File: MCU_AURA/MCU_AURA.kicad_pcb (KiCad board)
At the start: 4 copper layers, 50 x 50 mm, 110 parts, among them IC1 PCA9685PW,118, IC2 W25Q128JVSIQ, J1 TF-CARD_H1.8, J100 USB_C_Receptacle_USB2.0_16P, J400 532617004, J401 532617004, J402 532617004, J403 532617012, J404 532617007, J405 532617007, J406 532617012, J407 532617007, J408 532617004, Q300 BSS138, Q301 BSS138, Q302 BSS138, U100 TPS2115ADRBR, U101 TLV62566DBVR, U102 AP2127N-1.8, U200 ESP32-S3-WROOM-1, U201 USBLC6-2SC6, U300 ICM-20948, U301 BMP280

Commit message: Second Iteration MCU
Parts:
- added C205: 100n, Capacitor_SMD:C_0402_1005Metric, F.Cu at (112.5, 83.8)
- added C206: 100n, Capacitor_SMD:C_0402_1005Metric, F.Cu at (108.8, 81.5)
- added U202: TCAN1042VDRBRQ1, TCAN1042VDRBRQ1:DRB0008F, F.Cu at (109.5, 84.0)
- J400: renamed from J401; moved to F.Cu
- J401: renamed from J400; moved to B.Cu
- moved TP104 14.0 mm to (111.5, 88.0)
- moved R305 11.0 mm to (107.0, 80.2), turned to 0 degrees
- moved R104 10.6 mm to (107.0, 78.7), turned to 0 degrees
- moved R108 10.5 mm to (107.0, 76.9), turned to 0 degrees
- moved C305 10.2 mm to (107.0, 73.2), turned to 180 degrees
- moved D300 9.82 mm to (109.7, 80.2), turned to 0 degrees
- moved D103 9.46 mm to (109.7, 78.6), turned to 0 degrees
- moved D104 9.21 mm to (109.7, 76.9), turned to 0 degrees
- moved C304 7.96 mm to (107.0, 74.5), turned to 180 degrees
- moved U301 6.90 mm to (109.5, 74.2), turned to -90 degrees
- moved D409 2.76 mm to (106.8, 86.0), turned to -90 degrees
- moved D410 2.76 mm to (106.8, 82.0), turned to 90 degrees
- turned J400 to -90 degrees
- turned J401 to 90 degrees
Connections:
- J400 pad 2: SCL -> CANL
- J400 pad 3: SDA -> CANH
- U200 pad 24: unconnected-(U200-IO47-Pad24) -> /200_ESP32/CAN_RX
- U200 pad 25: unconnected-(U200-IO48-Pad25) -> /200_ESP32/CAN_TX
- U200 pad 26: unconnected-(U200-IO45-Pad26) -> /200_ESP32/CAN_STB
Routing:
- net /200_ESP32/CAN_STB: track 0.00 -> 32.4 mm, vias 0 -> 2
- net /200_ESP32/CAN_TX: track 0.00 -> 27.2 mm, vias 0 -> 2
- net /200_ESP32/CAN_RX: track 0.00 -> 26.0 mm, vias 0 -> 2
- net SDA: track 93.9 -> 101.8 mm
- net LED: track 30.0 -> 23.7 mm, vias 2 -> 4
- net SCL: track 94.0 -> 99.9 mm, vias 6 -> 7
- net CANL: track 0.00 -> 3.88 mm
- net CANH: track 0.00 -> 3.16 mm
- net +3V3: track 51.9 -> 53.6 mm, vias 36 -> 37
- net /200_ESP32/USB_MCU_D-: track 21.1 -> 20.6 mm
- net /200_ESP32/USB_MCU_D+: track 21.1 -> 20.6 mm
- net GND: track 76.2 -> 76.1 mm, vias 155 -> 150
- net MOSI: track 57.6 -> 57.7 mm, vias 6 -> 5

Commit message: Production Files for MCU
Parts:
- R104: value 4k7 -> 1k
- R106: value 68k -> 6k8
- R107: value 15k -> 1k5
- R108, R305: value 1k -> 470R
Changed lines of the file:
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@@
 		(allow_soldermask_bridges_in_footprints no)
 		(tenting front back)
+		(grid_origin 100 100)
 		(pcbplotparams
 			(layerselection 0x00000000_00000000_55555555_575575ff)
@@
 			(drillshape 0)
 			(scaleselection 1)
-			(outputdirectory "C:/Users/Alexander_Armitage/Desktop/Initial_Quote/")
+			(outputdirectory "Gerber/")
 		)
 	)
@@
 			)
 		)
-		(property "Value" "15k"
+		(property "Value" "1k5"
 			(at 0 1.17 90)
 			(layer "F.Fab")
@@
 			)
 		)
-		(property "Value" "1k"
+		(property "Value" "470R"
 			(at -0.7125 -1.83 0)
 			(layer "F.Fab")
@@
 			)
 		)
-		(property "Value" "68k"
+		(property "Value" "6k8"
 			(at 0 1.17 90)
 			(layer "F.Fab")
@@
 			)
 		)
-		(property "Value" "1k"
+		(property "Value" "470R"
 			(at 0 1.17 0)
 			(layer "F.Fab")
@@
 			)
 		)
-		(property "Value" "4k7"
+		(property "Value" "1k"
 			(at -0.7125 -1.83 0)
 			(layer "F.Fab")

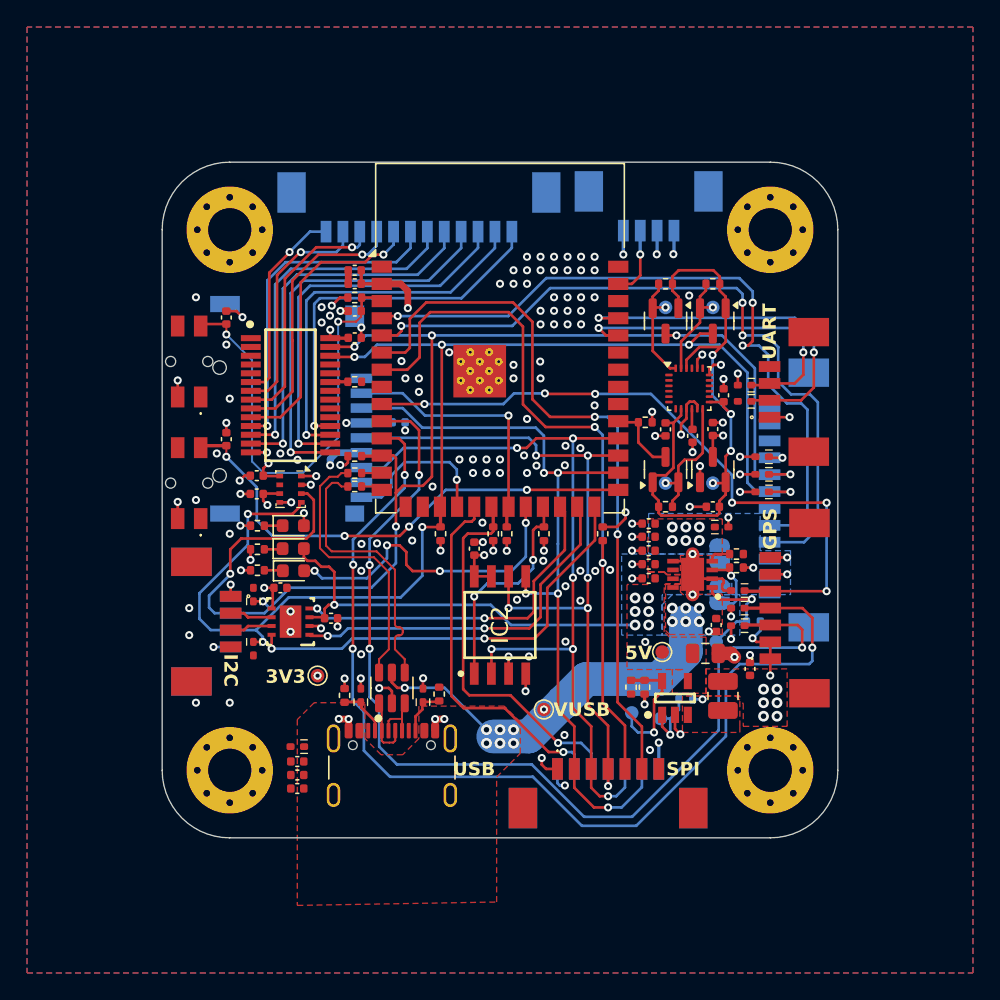
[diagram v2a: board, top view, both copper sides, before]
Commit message: CPL file finalised for MCU
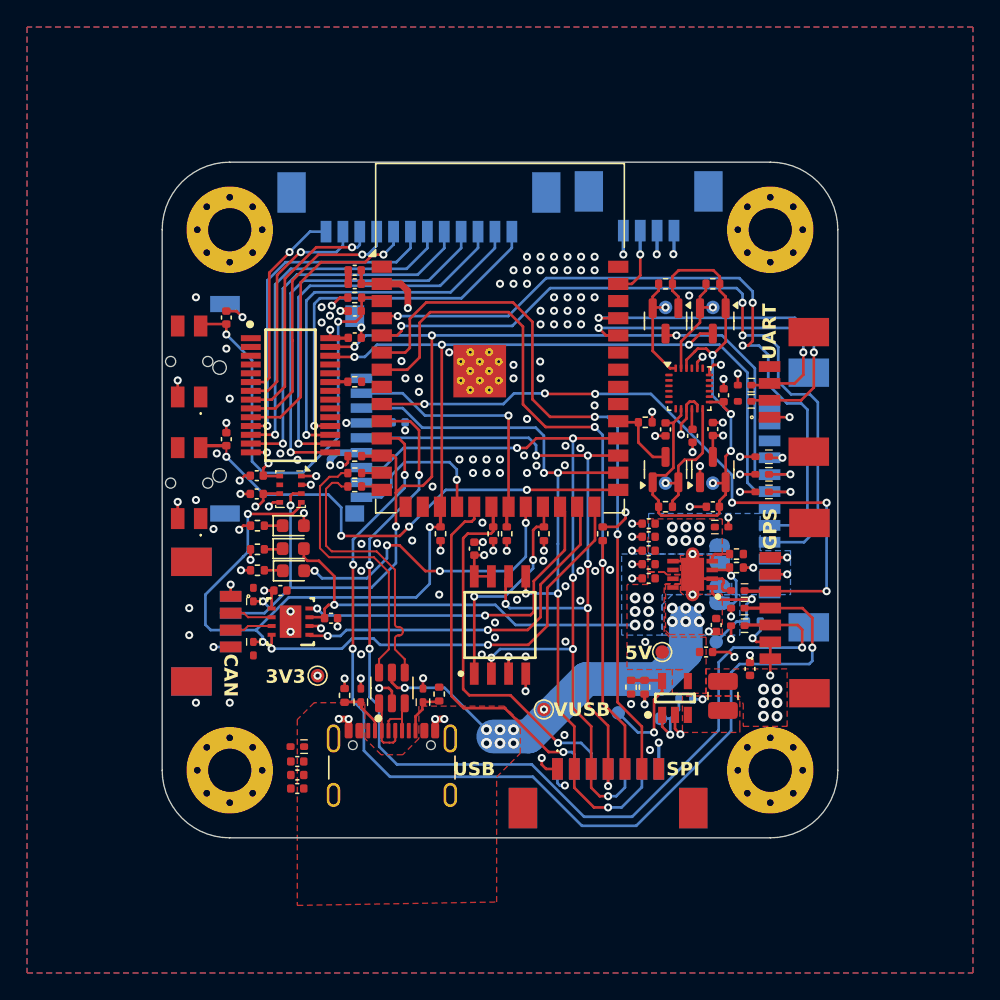
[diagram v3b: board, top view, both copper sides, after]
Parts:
- C106: footprint Capacitor_SMD:C_0805_2012Metric -> Capacitor_SMD:C_0402_1005Metric
- moved TP103 1.00 mm to (133.8, 90.8)
- moved C206 0.20 mm to (108.8, 81.7)
- moved C106 0.11 mm to (140.2, 86.2)
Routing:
- net SDA: track 101.8 -> 92.6 mm
- net GND: track 76.1 -> 76.7 mm, vias 150 -> 155
- net LED: track 23.7 -> 23.1 mm
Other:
- board text added: "CAN"
- board text added: "RC"

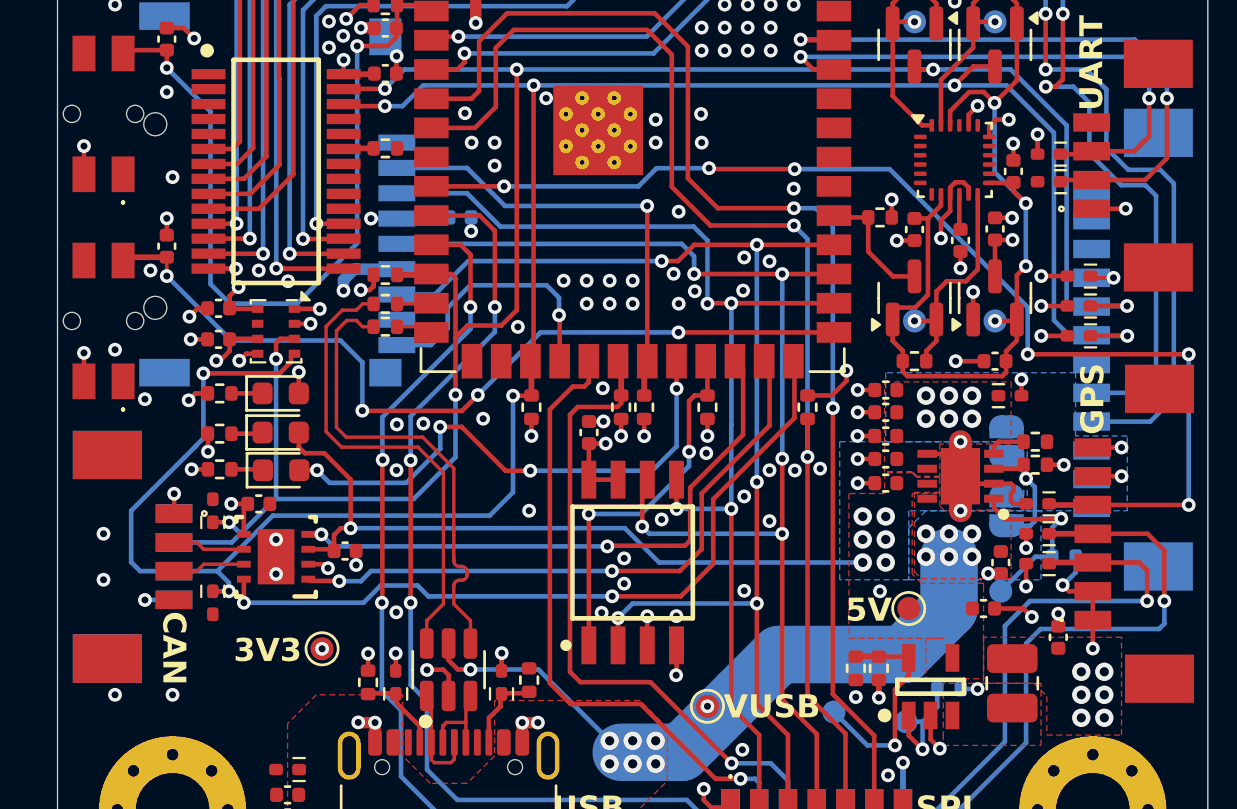
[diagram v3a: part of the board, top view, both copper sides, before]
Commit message: Silk Screen Done
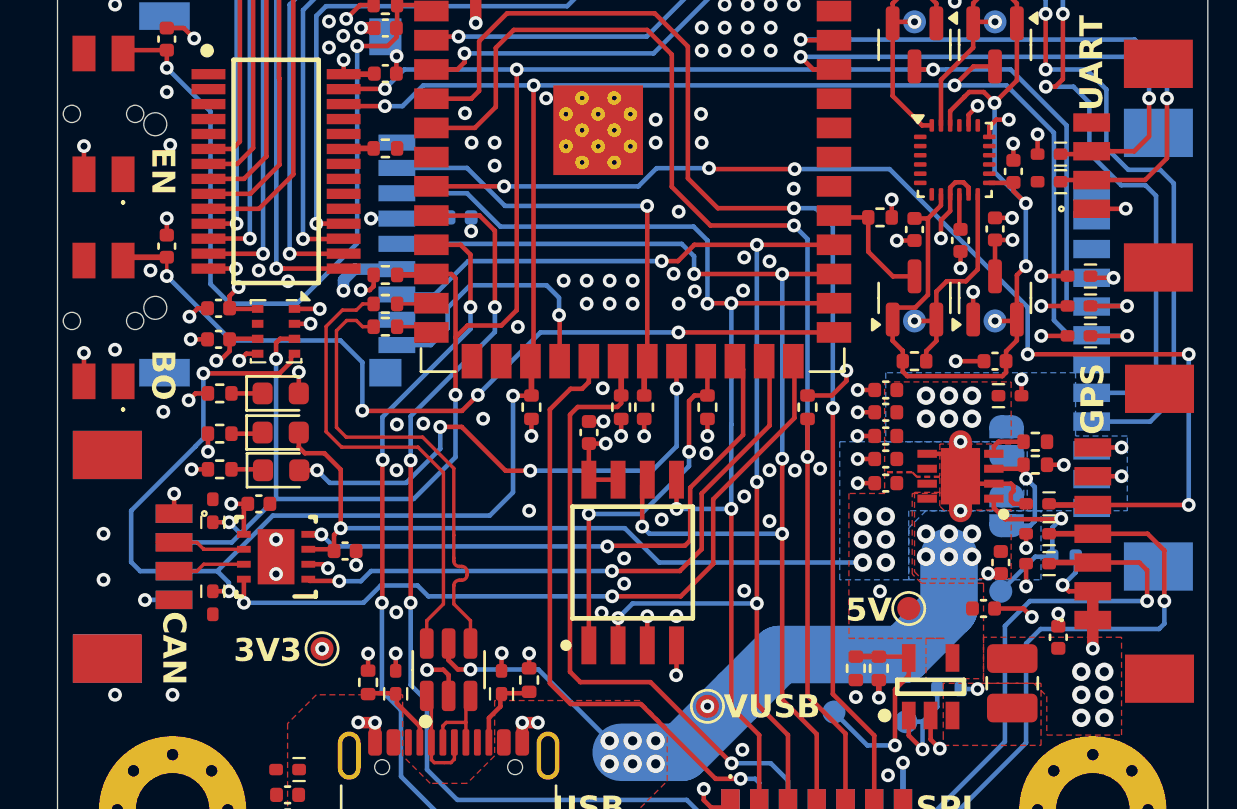
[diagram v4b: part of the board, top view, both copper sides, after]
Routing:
- net GND: track 76.7 -> 77.4 mm, vias 155 -> 156
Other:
- board text added: "AURA MCU"
- board text added: "Alexander Armitage"
- board text added: "BO"
- board text added: "EN"
- board text added: "V0.0.1"

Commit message: First Order
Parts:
- moved J100 0.15 mm to (117.0, 95.9)
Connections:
- U200 pad 26: /200_ESP32/CAN_STB -> unconnected-(U200-IO45-Pad26)
- U202 pad 8: /200_ESP32/CAN_STB -> GND
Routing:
- net /200_ESP32/CAN_STB: track 32.8 -> 0.00 mm, vias 2 -> 0
- net /200_ESP32/CAN_TX: track 27.2 -> 28.0 mm
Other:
- board text added: "V1.0"
- board text removed: "V0.0.1"
